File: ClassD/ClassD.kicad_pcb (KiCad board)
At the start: 2 copper layers, 83.6 x 45.3 mm, 37 parts, among them J1 RCJ-01X, J2 RCJ-01X, P1 CONN_01X02, SW1 FSM2JSMAA, U1 AP1117E50G-13, U2 TPA2008D2

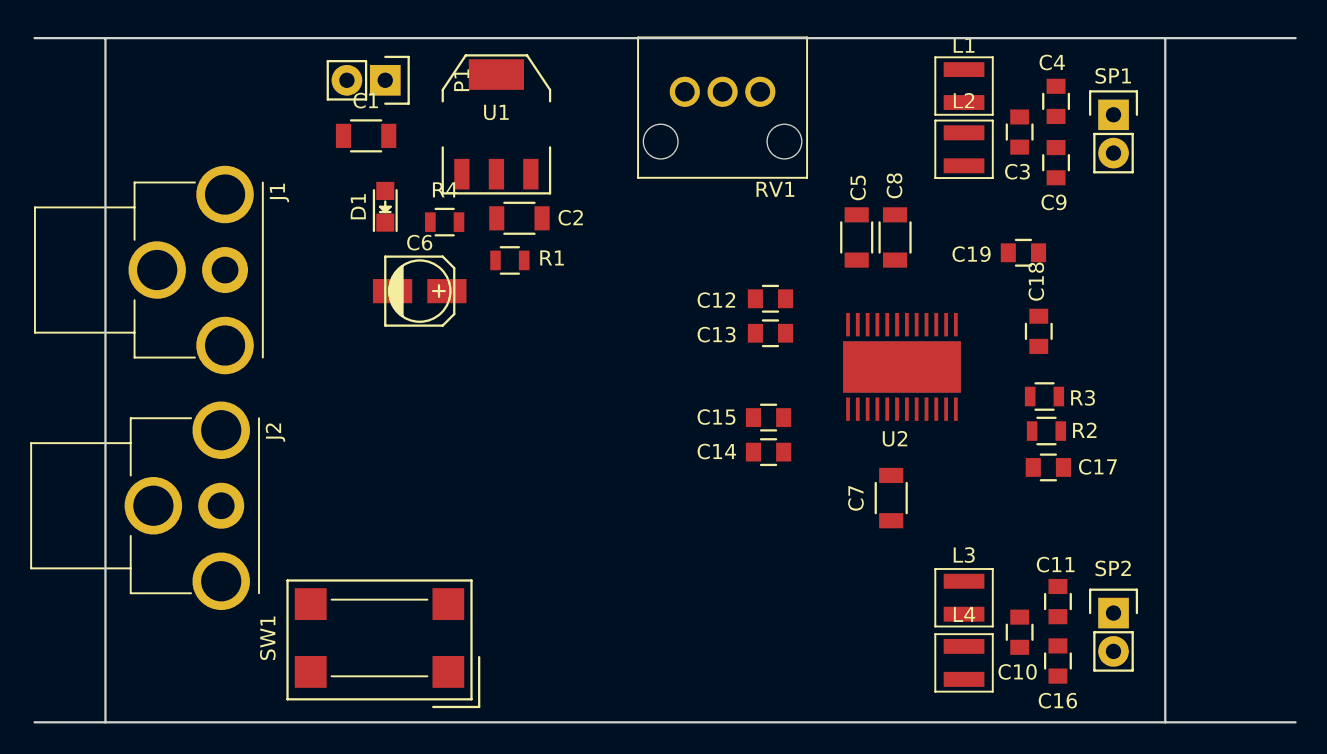
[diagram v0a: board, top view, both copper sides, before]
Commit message: Added the GND Zones and started routing
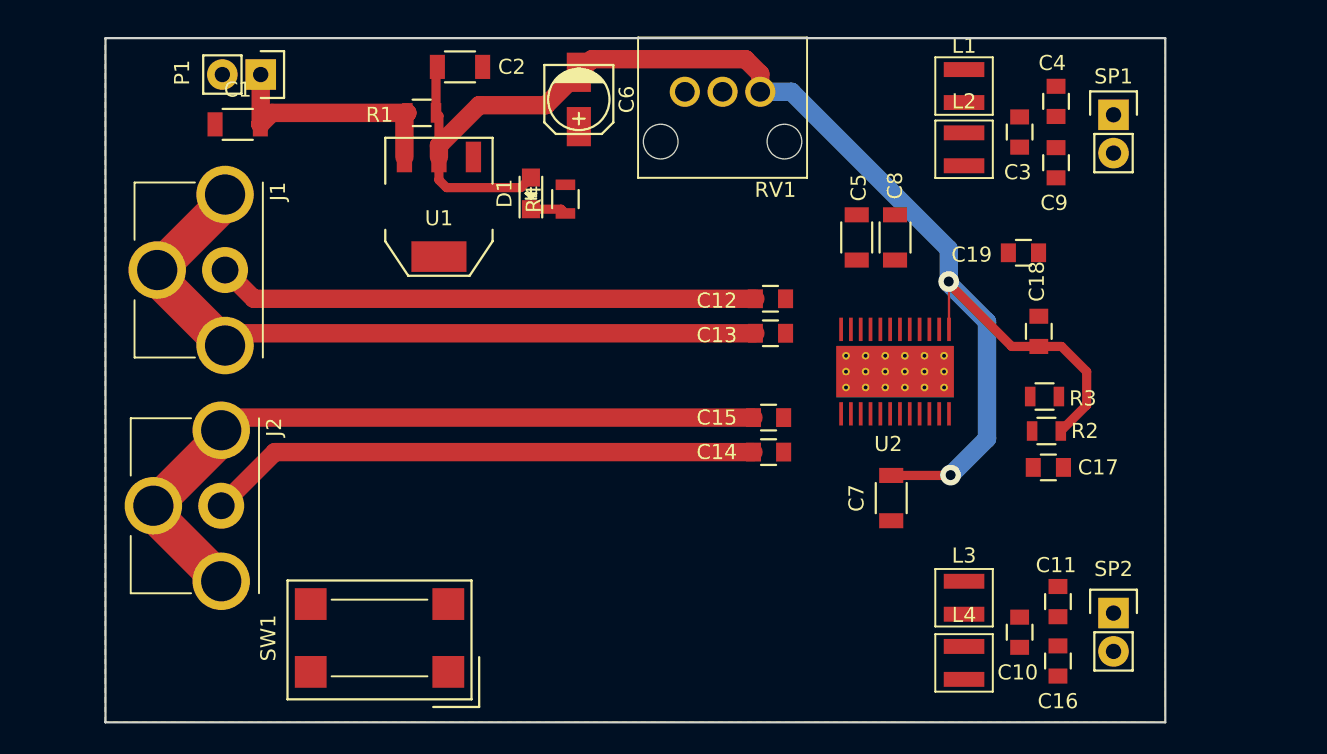
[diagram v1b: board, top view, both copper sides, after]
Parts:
- moved C6 16.5 mm to (124.3, 86.6), turned to 270 degrees
- moved R1 11.4 mm to (113.9, 87.5), turned to 180 degrees
- moved C2 10.8 mm to (116.5, 84.5)
- moved D1 9.69 mm to (121.2, 92.8)
- moved C1 8.54 mm to (101.7, 88.3)
- moved P1 8.26 mm to (103.3, 85.0)
- moved R4 8.14 mm to (123.4, 93.2), turned to 90 degrees
- moved U1 6.66 mm to (115.1, 93.7), turned to 180 degrees
- moved U2 0.55 mm to (145.3, 104.6)
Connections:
- C6 pad 2: /LOUTP -> /VDD
- C7 pad 2: /LOUTP -> /VDD
- U2 pad 9: /LOUTP -> /VDD
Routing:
- net /VDD: track 0.00 -> 97.4 mm, vias 0 -> 2
- net /LIN-: track 0.00 -> 49.4 mm
- net /RIN-: track 0.00 -> 49.2 mm
- net /LIN+: track 0.00 -> 36.7 mm
- net /RIN+: track 0.00 -> 35.9 mm
- net /VIN: track 0.00 -> 16.4 mm
- net Net-(D1-Pad1): track 0.00 -> 2.40 mm
- added copper zone on B.Cu, net GND
- added copper zone on F.Cu, net GND
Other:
- board size 83.6 x 45.3 mm -> 70.2 x 45.3 mm
- net class Default: clearance 0.2 -> 0.1524; trace_width 0.25 -> 0.1524; via_dia 0.6 -> 0.6858; via_drill 0.4 -> 0.3302
- rule trace_clearance: 0.2 -> 0.1524
- rule trace_min: 0.2 -> 0.1524
- rule via_min_drill: 0.3 -> 0.3302
- rule via_min_size: 0.4 -> 0.6858

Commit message: updated the layout
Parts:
- moved L4 6.77 mm to (152.5, 117.7), turned to 270 degrees
- moved C16 4.19 mm to (156.0, 119.6)
- moved C7 3.81 mm to (141.7, 114.9)
- moved C11 3.81 mm to (156.0, 123.7)
- moved C10 3.36 mm to (150.2, 121.3), turned to 180 degrees
- moved L3 2.52 mm to (148.2, 117.7), turned to 90 degrees
- moved C17 2.42 mm to (155.3, 108.6)
- moved SP2 2.32 mm to (159.4, 122.9), turned to 180 degrees
- moved R2 2.29 mm to (155.2, 110.9)
- moved C8 1.14 mm to (146.4, 95.8), turned to 270 degrees
- moved R3 0.13 mm to (155.1, 106.3)
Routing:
- net /~SHUTDOWN: track 0.00 -> 47.5 mm, vias 0 -> 2
- net /VOLUME: track 0.00 -> 34.6 mm, vias 0 -> 1
- net Net-(L1-Pad1): track 0.00 -> 21.2 mm
- net /LOUT+: track 0.00 -> 16.8 mm
- net Net-(L2-Pad1): track 0.00 -> 14.9 mm
- net Net-(L4-Pad1): track 0.00 -> 13.8 mm
- net /LOUT-: track 0.00 -> 13.8 mm
- net /VDD: track 97.4 -> 111.2 mm
- net /LOUTP: track 0.00 -> 11.4 mm
- net /ROUT-: track 0.00 -> 10.5 mm
- net /ROUT+: track 0.00 -> 10.4 mm
- net Net-(C17-Pad1): track 0.00 -> 10.1 mm
- net Net-(R3-Pad1): track 0.00 -> 9.73 mm
- net Net-(C14-Pad1): track 0.00 -> 6.25 mm
- net Net-(C12-Pad1): track 0.00 -> 5.99 mm
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
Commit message: Wrapping up the routing
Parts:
- D1: footprint LEDs:LED_0805 -> LoudMouth-ClassD:LED_0805
- moved C2 3.18 mm to (113.3, 84.6), turned to 0 degrees
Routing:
- net /VDD: track 111.2 -> 132.7 mm, vias 2 -> 4
- net Net-(C8-Pad2): track 4.81 -> 10.2 mm, vias 0 -> 2

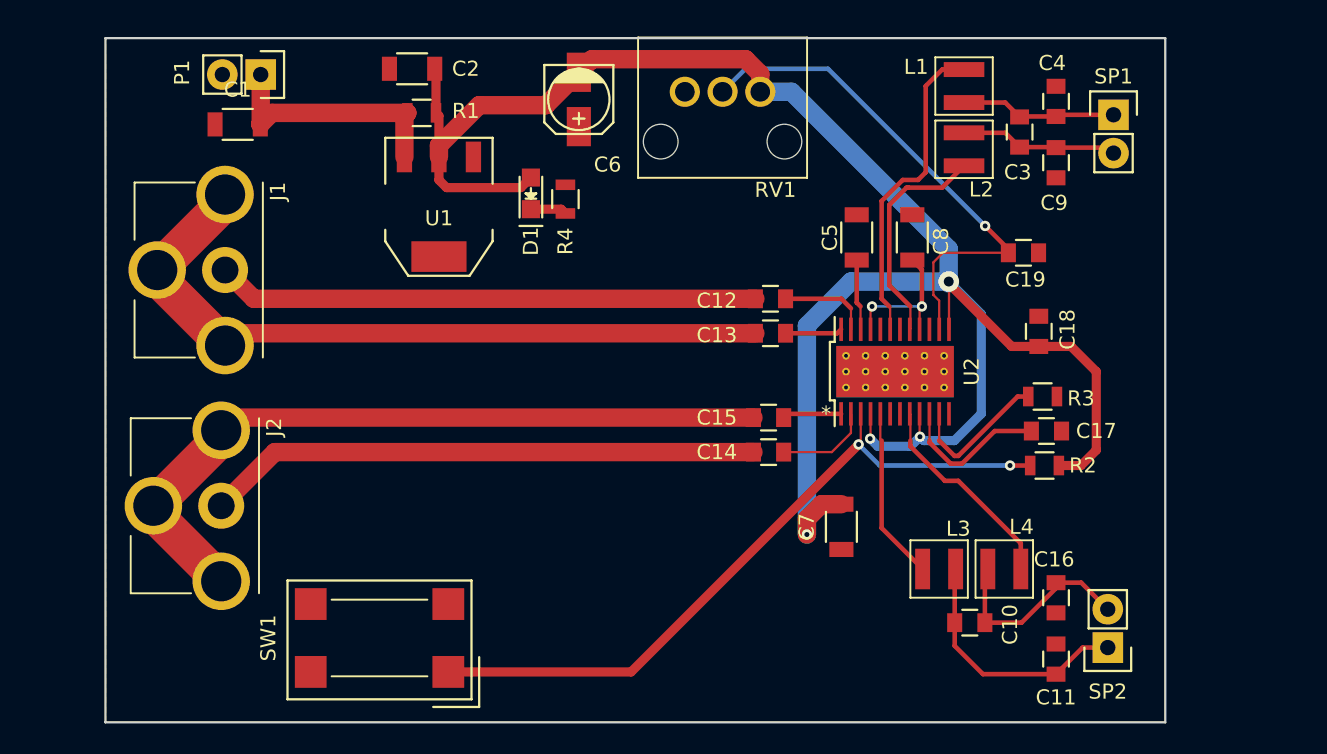
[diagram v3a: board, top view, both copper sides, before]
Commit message: Added the logos and revision text
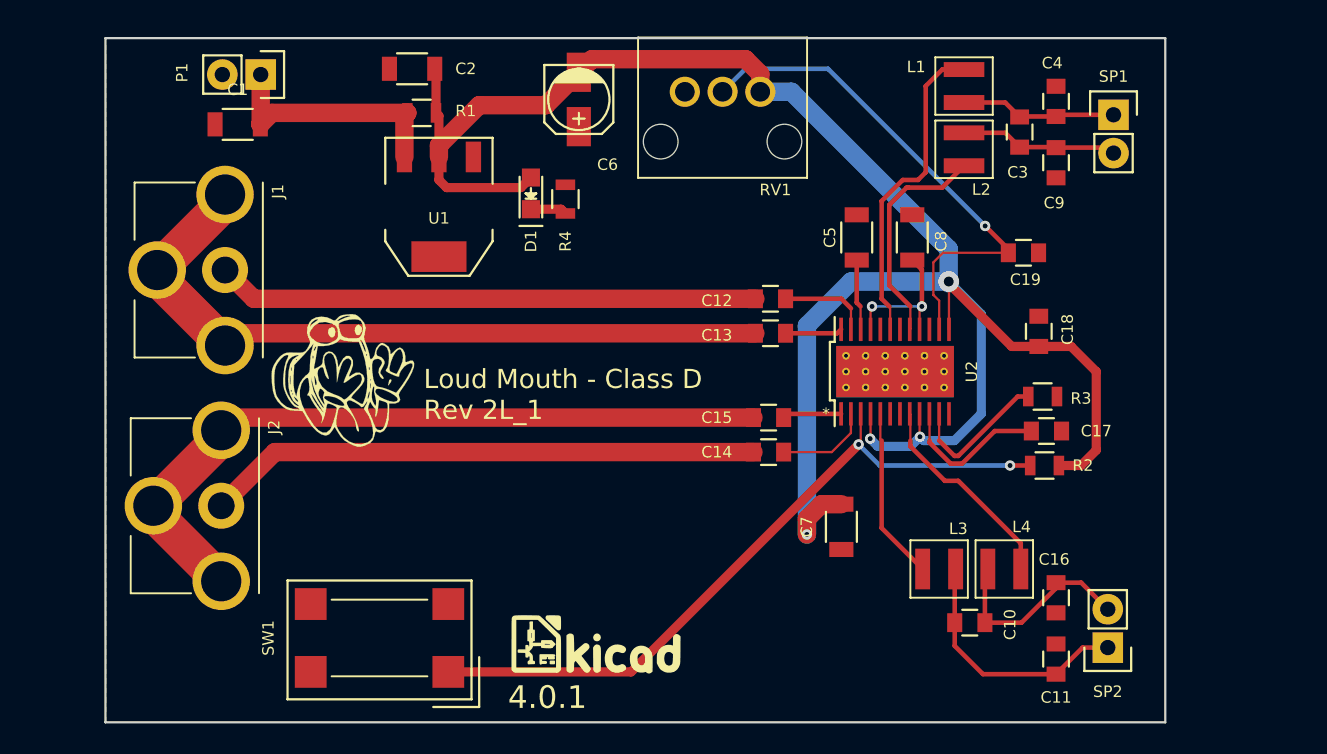
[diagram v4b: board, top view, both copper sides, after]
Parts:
- added G***: LOGO, LoudMouth-ClassD:LoudMouth_Logo_10, F.Cu at (108.7, 105.2)
- added G***: LOGO, LoudMouth-ClassD:KiCad-Logo, F.Cu at (125.5, 122.7)
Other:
- board text added: "4.0.1"
- board text added: "Loud Mouth - Class D Rev 2L_1"

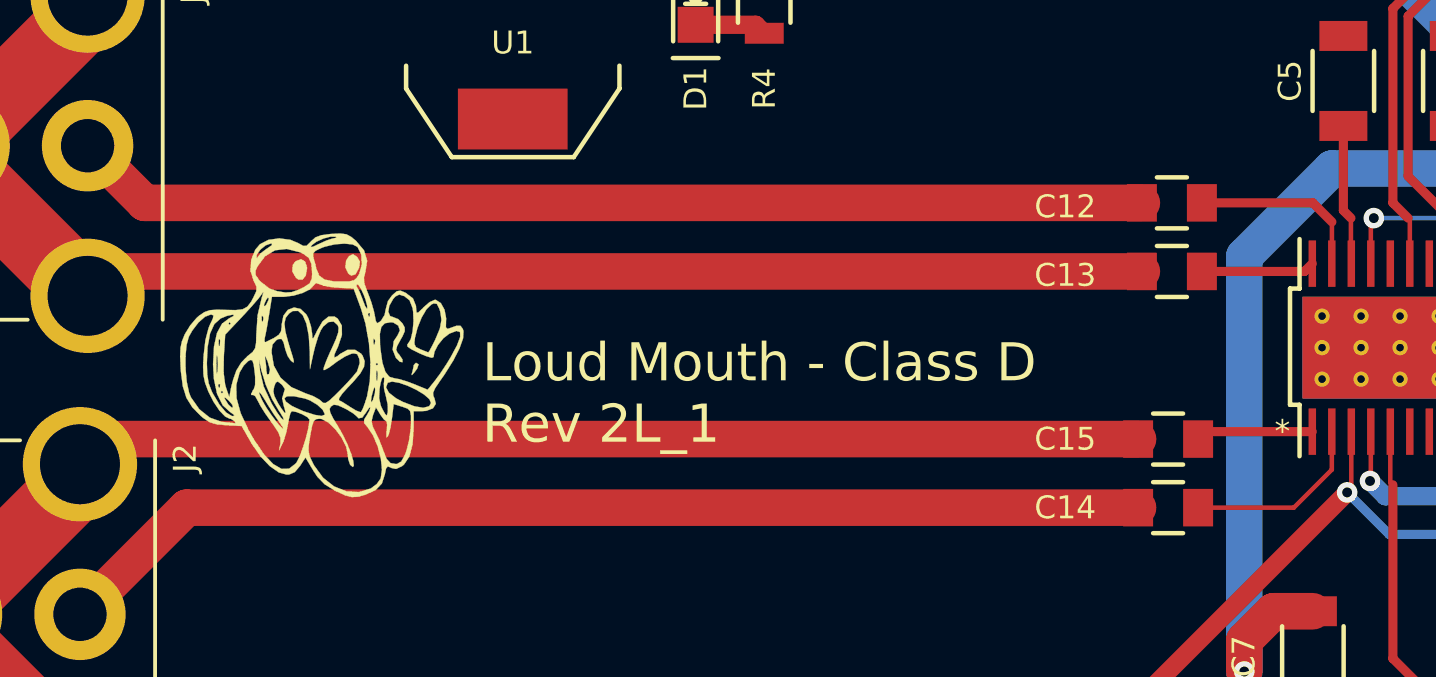
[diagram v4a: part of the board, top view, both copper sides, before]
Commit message: Fininalised the logos
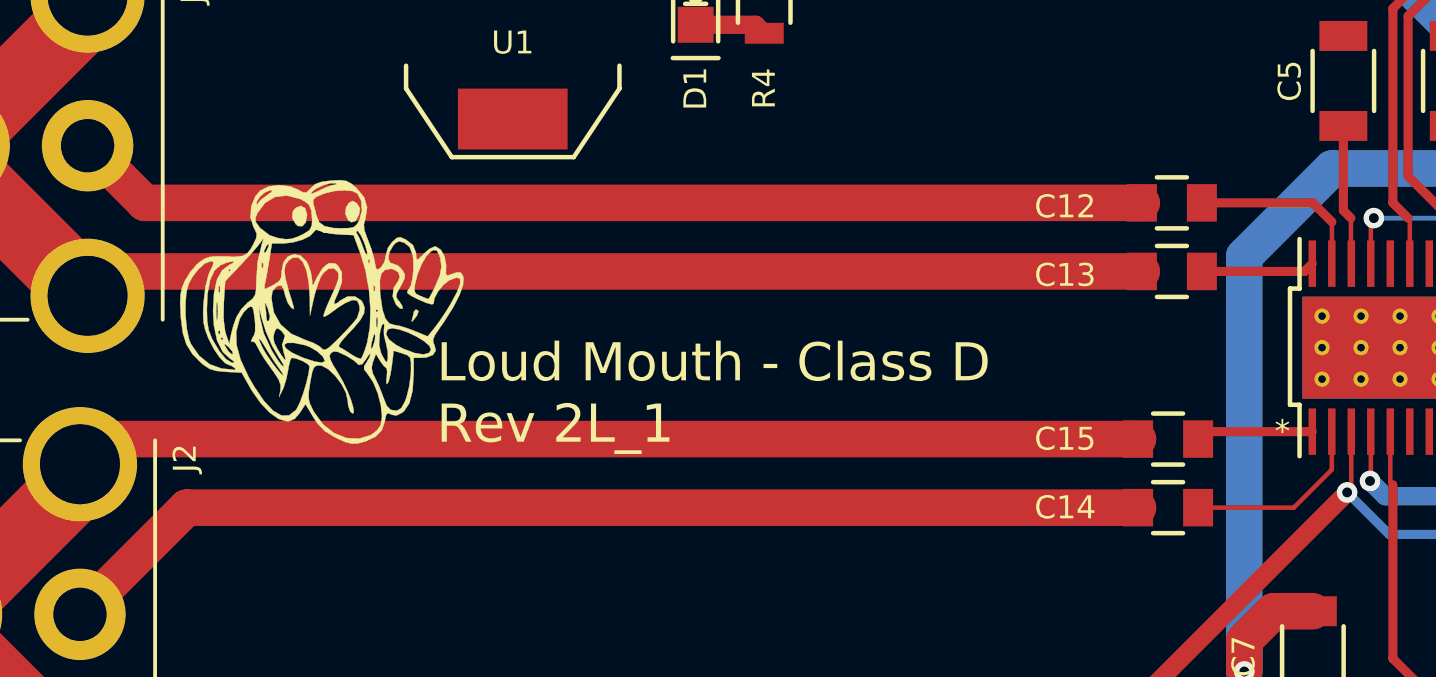
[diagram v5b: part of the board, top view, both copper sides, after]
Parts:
- LOGO1: renamed from G***; value LOGO -> LoudMouth_10
- LOGO2: renamed from G***; value LOGO -> KiCad
- moved LOGO1 1.78 mm to (108.7, 103.4)
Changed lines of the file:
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@@
     (links 95)
     (no_connects 0)
-    (area 92.888999 82.474999 163.270001 127.964001)
+    (area 87.823099 73.690099 163.270001 127.964001)
     (thickness 1.6)
     (drawings 6)
@@
   )
   (module LoudMouth-ClassD:LoudMouth_Logo_10 (layer F.Cu)
-    (at 108.712 105.156)
-    (fp_text reference G*** (at 0 0) (layer F.SilkS) hide
-      (effects (font (size 0.762 0.762) (thickness 0.127)))
-    )
-    (fp_text value LOGO (at 0.75 0) (layer F.SilkS) hide
+    (at 108.712 103.378)
+    (fp_text reference LOGO1 (at 0 0) (layer F.SilkS) hide
+      (effects (font (size 0.762 0.762) (thickness 0.127)))
+    )
+    (fp_text value LoudMouth_10 (at 0.75 0) (layer F.SilkS) hide
       (effects (font (size 0.762 0.762) (thickness 0.127)))
     )
@@
   (module LoudMouth-ClassD:KiCad-Logo (layer F.Cu)
     (at 125.476 122.682)
-    (fp_text reference G*** (at 0 0) (layer F.SilkS) hide
+    (fp_text reference LOGO2 (at 0 0) (layer F.SilkS) hide
       (effects (font (thickness 0.3)))
     )
-    (fp_text value LOGO (at 0.75 0) (layer F.SilkS) hide
+    (fp_text value KiCad (at 0.75 0) (layer F.SilkS) hide
       (effects (font (thickness 0.3)))
     )
@@
     (effects (font (size 1.5 1.5) (thickness 0.3)) (justify left))
   )
-  (gr_text "Loud Mouth - Class D\nRev 2L_1" (at 114.046 106.172) (layer F.SilkS)
+  (gr_text "Loud Mouth - Class D\nRev 2L_1" (at 112.522 106.172) (layer F.SilkS)
     (effects (font (size 1.27 1.27) (thickness 0.254)) (justify left))
   )
